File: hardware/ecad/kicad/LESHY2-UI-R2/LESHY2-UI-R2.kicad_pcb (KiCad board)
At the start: 6 copper layers, 80 x 150 mm, 432 parts, among them J1 Hirose FH34SRJ-50S-0.5SH(50), J10 Samtec FTSH-105-01-L-DV-K-P-TR, J11 GCT USB4105-GF-A, J12 GCT RFPC-SMA31-FN-175-A, J13 Hirose U.FL-R-SMT-1(80), J14 GCT RFPC-SMA31-FN-175-A, J15 Hirose U.FL-R-SMT-1(80), J16 GCT RFPC-SMA31-FN-175-A, J17 Hirose U.FL-R-SMT-1(80), J18 Hirose FX8C-80P-SV1(92), J2 Samtec FTSH-105-01-L-DV-K-P-TR, J3 GCT RFPC-SMA32-FN-175-A, J4 Hirose U.FL-R-SMT-1(80), J5 Hirose DM3AT-SF-PEJM5, J6 Samtec FTSH-105-01-L-DV-K-P-TR, J7 GCT RFPC-SMA32-FN-175-A, J8 Hirose U.FL-R-SMT-1(80), J9 GCT USB4105-GF-A, Q1 Diodes Incorporated DMN2056U-7, Q2 Diodes Incorporated 2N7002DW-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, Q3 Diodes Incorporated DMN2056U-7, Q4 Diodes Incorporated DMN2056U-7, Q5 Diodes Incorporated DMN2056U-7, Q6 Diodes Incorporated 2N7002DW-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, SW1 Alps Alpine SKRTLAE010, SW10 OMRON B3S-1100P, SW11 OMRON B3S-1100P, SW12 OMRON B3S-1100P, SW13 OMRON B3S-1100P, SW14 OMRON B3S-1100P, SW15 OMRON B3S-1100P, SW16 OMRON B3S-1100P, SW17 OMRON B3S-1100P, SW18 Alps Alpine SKRTLAE010, SW19 Alps Alpine SKRTLAE010, SW2 Alps Alpine SKRTLAE010, SW20 Alps Alpine SKRTLAE010, SW21 Alps Alpine SKRTLAE010, SW3 OMRON B3S-1100P, SW4 OMRON B3S-1100P, SW5 OMRON B3S-1100P, SW6 OMRON B3S-1100P, SW7 OMRON B3S-1100P, SW8 OMRON B3S-1100P, SW9 OMRON B3S-1100P, U1 ESP32-S3-WROOM-1U-N16R8, U10 Texas Instruments TPS22919DCKR, U11 SN74LVC1G07DCKR, U12 Texas Instruments TPD8E003DQDR, U13 TCA9539PWR, U14 ESP32-C5-WROOM-1U-N8R8, U15 Texas Instruments TPD4E05U06D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, U16 KYOCERA AVX CP0603Q5425ENTR, U17 74LVC2G14GV,125, U18 SN74LVC1G74DCUR, U19 74HC20PW,118, U2 Texas Instruments TPD4E05U06D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, U20 74LVC2G14GV,125, U21 Texas Instruments TPD2EUSB30A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, U22 onsemi FSUSB42MUX, U23 Vishay TSMP95000TR, U24 Vishay TSOP75238TR, U25 Texas Instruments TPS22919DCKR, U26 Nexperia 74LVC2G126DP,125, U27 SN74LVC1G08DCKR, U28 SC1512-A4, U29 Texas Instruments TPD4E05U06D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, U3 KYOCERA AVX CP0603Q5425ENTR, U30 Texas Instruments TPD2EUSB30A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, U31 onsemi FSUSB42MUX, U32 Analog Devices AD8314ARMZ-REEL, U33 Analog Devices AD8314ARMZ-REEL, U34 Analog Devices AD8314ARMZ-REEL, U35 Ebyte E01-ML01SP4, U36 TTM Technologies DC2337J5010A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, U37 Nexperia 74LVC126APW,118, U38 Nexperia 74LVC2G126DP,125, U39 Ebyte E01-ML01SP4, U4 Texas Instruments TPS2553DRVR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, U40 TTM Technologies DC2337J5010A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

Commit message: Protect C5 shared USB pair and document mux control gap
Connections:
- net /UI_20_C5_WIFI_IR_SERVICE/C5_GPIO13_COMMON renamed /UI_20_C5_WIFI_IR_SERVICE/C5_USB_SDIO_COMMON_N
- net /UI_20_C5_WIFI_IR_SERVICE/C5_GPIO14_COMMON renamed /UI_20_C5_WIFI_IR_SERVICE/C5_USB_SDIO_COMMON_P
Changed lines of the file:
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@@
 			(layers "B.Cu" "B.Mask" "B.Paste")
 			(roundrect_rratio 0.25)
-			(net "/UI_20_C5_WIFI_IR_SERVICE/C5_GPIO14_COMMON")
+			(net "/UI_20_C5_WIFI_IR_SERVICE/C5_USB_SDIO_COMMON_P")
 		)
 		(pad "4" smd roundrect
@@
 			(layers "B.Cu" "B.Mask" "B.Paste")
 			(roundrect_rratio 0.25)
-			(net "/UI_20_C5_WIFI_IR_SERVICE/C5_GPIO13_COMMON")
+			(net "/UI_20_C5_WIFI_IR_SERVICE/C5_USB_SDIO_COMMON_N")
 		)
 		(pad "5" smd roundrect
@@
 			(layers "B.Cu" "B.Mask" "B.Paste")
 			(roundrect_rratio 0.2)
-			(net "/UI_20_C5_WIFI_IR_SERVICE/C5_GPIO13_COMMON")
+			(net "/UI_20_C5_WIFI_IR_SERVICE/C5_USB_SDIO_COMMON_N")
 		)
 		(pad "14" smd roundrect
@@
 			(layers "B.Cu" "B.Mask" "B.Paste")
 			(roundrect_rratio 0.2)
-			(net "/UI_20_C5_WIFI_IR_SERVICE/C5_GPIO14_COMMON")
+			(net "/UI_20_C5_WIFI_IR_SERVICE/C5_USB_SDIO_COMMON_P")
 		)
 		(pad "15" smd roundrect

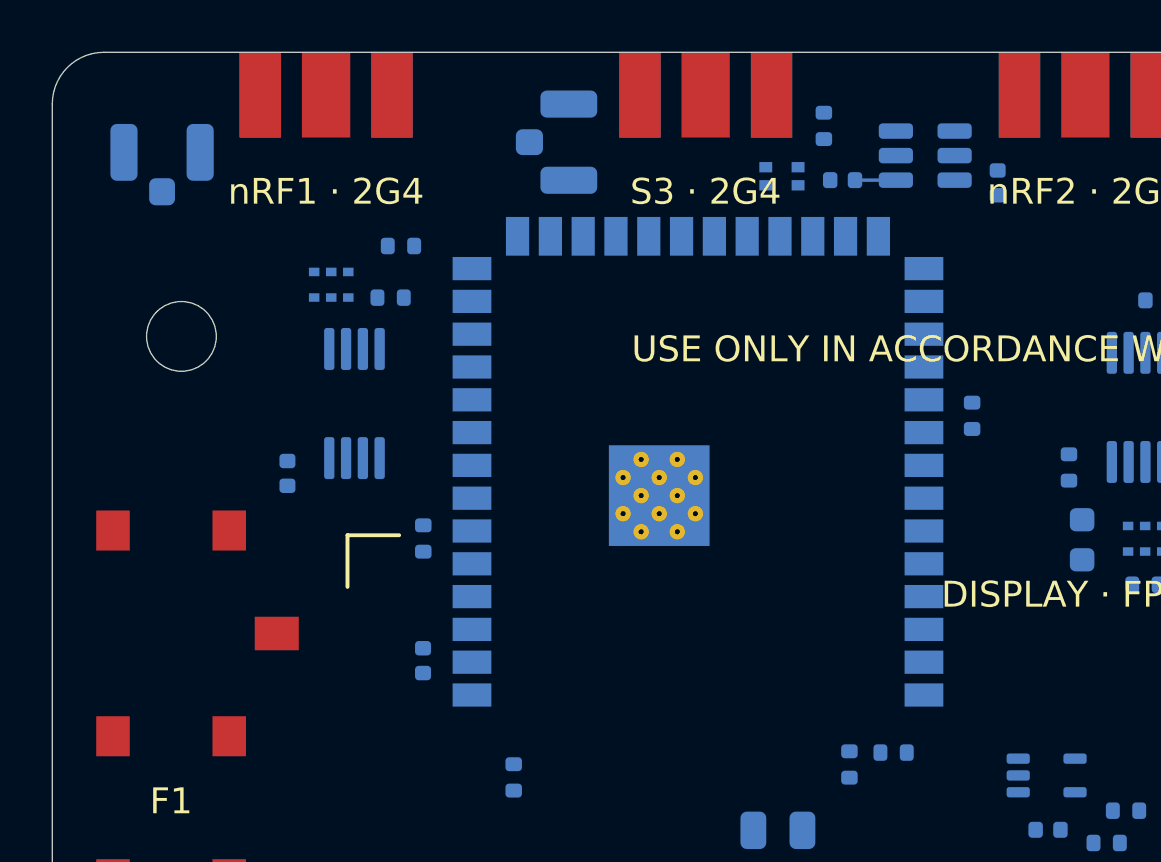
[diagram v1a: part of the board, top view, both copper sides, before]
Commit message: Clear SMA solder access with bounded support relocations
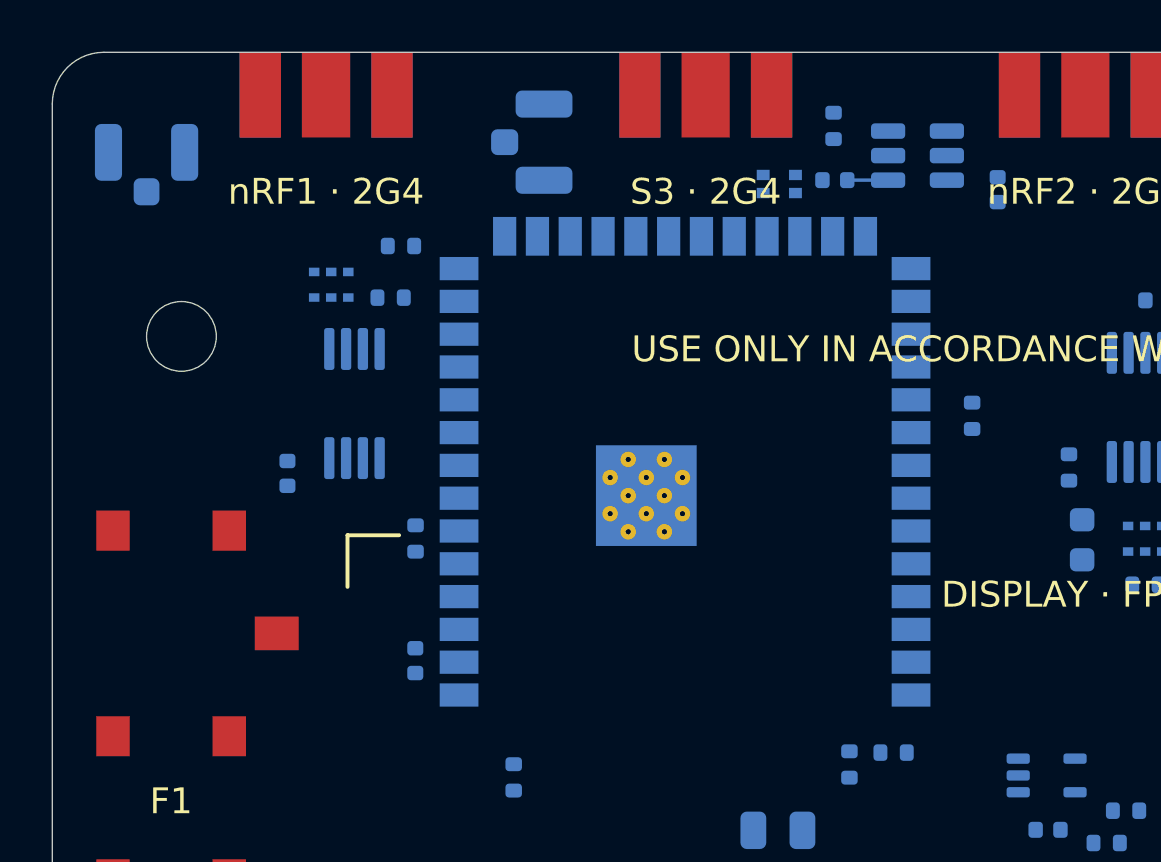
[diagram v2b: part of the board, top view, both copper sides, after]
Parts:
- moved J4 0.96 mm to (19.0, 3.48)
- moved J13 0.60 mm to (3.65, 3.88)
- moved U1 0.50 mm to (24.5, 16.5)
- moved R17 0.38 mm to (30.2, 2.85)
- moved U3 0.32 mm to (28.1, 5.10)
- moved C2 0.30 mm to (30.3, 4.95)
- moved C6 0.30 mm to (14.1, 23.6)
- moved R12 0.30 mm to (14.1, 18.8)
- moved U52 0.30 mm to (33.5, 4.00)
- moved C1 0.27 mm to (36.6, 5.32)

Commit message: fix(hardware): correct native placement and publish verified component views
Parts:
- moved C7 48.8 mm to (43.9, 40.4), turned to -90 degrees
- moved C15 45.3 mm to (66.8, 128.3), turned to 0 degrees
- moved C16 42.3 mm to (62.2, 130.3)
- moved C62 40.6 mm to (4.55, 52.2), turned to 180 degrees
- moved C63 32.0 mm to (5.17, 53.7), turned to 180 degrees
- moved C74 18.6 mm to (57.3, 62.0), turned to -90 degrees
- moved C68 17.3 mm to (30.1, 47.9), turned to 90 degrees
- moved C75 16.9 mm to (51.1, 57.6), turned to 180 degrees
- moved C69 14.8 mm to (29.9, 50.1), turned to 180 degrees
- moved C17 10.6 mm to (40.8, 78.4), turned to -90 degrees
- moved R18 10.0 mm to (53.9, 40.3), turned to 0 degrees
- moved R99 7.21 mm to (44.3, 60.1), turned to 180 degrees
- moved R198 6.28 mm to (44.8, 58.4), turned to 90 degrees
- moved R42 4.28 mm to (61.6, 126.1), turned to 90 degrees
- moved C54 0.30 mm to (14.8, 136.9)
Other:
- board text added: "SPEAKER / ASSEMBLY"

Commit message: Restore microphone to RF-inner bottom edge and align front label
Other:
- board text added: "MIC"
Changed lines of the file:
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@@
+		)
+	)
+	(gr_text "MIC"
+		(at 33 148.9 0)
+		(layer "F.SilkS")
+		(effects
+			(font
+				(size 1 1)
+				(thickness 0.15)
+			)
 		)
 	)

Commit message: Complete native interface silkscreen with verified local clearances
Add 29 real front/back labels and independently cover 76 interfaces / 95 required captions. Move eight reviewed unrouted RF resistors while preserving all native copper and named pad connectivity. Refresh four-face, exterior, and routing visuals; keep H6.0.3-R1 open.

Validation: system suite 1459 tests OK (114 skips in system Python); KiCad H6 suite 863 tests OK, no skips. Both native DRC reports have zero violations and zero schematic-parity errors. Current routing remains incomplete.
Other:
- board text added: "C5 ANT"
- board text added: "C5 DBG"
- board text added: "DISPLAY"
- board text added: "HUB DBG"
- board text added: "IR LRN"
- board text added: "IR RX"
- board text added: "IR TX"
- board text added: "M1 UI"
- board text added: "S3 ANT"
- board text added: "S3 DBG"
- board text added: "nRF1 ANT"
- board text added: "nRF2 ANT"
- board text added: "nRF3 ANT"
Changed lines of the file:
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@@
+		)
+	)
+	(gr_text "IR RX"
+		(at 4.5 78.1 0)
+		(layer "F.SilkS")
+		(effects
+			(font
+				(size 1 1)
+				(thickness 0.15)
+			)
+		)
+	)
+	(gr_text "IR LRN"
+		(at 4.5 85.6 0)
+		(layer "F.SilkS")
+		(effects
+			(font
+				(size 1 1)
+				(thickness 0.15)
+			)
+		)
+	)
+	(gr_text "IR TX"
+		(at 4.5 92 0)
+		(layer "F.SilkS")
+		(effects
+			(font
+				(size 1 1)
+				(thickness 0.15)
+			)
+		)
+	)
+	(gr_text "S3 DBG"
+		(at 3.075 109.6 0)
+		(layer "B.SilkS")
+		(effects
+			(font
+				(size 1 1)
+				(thickness 0.15)
+			)
+			(justify mirror)
+		)
+	)
+	(gr_text "nRF1 ANT"
+		(at 5 7.65 0)
+		(layer "B.SilkS")
+		(effects
+			(font
+				(size 1 1)
+				(thickness 0.15)
+			)
+			(justify mirror)
+		)
+	)
+	(gr_text "S3 ANT"
+		(at 24.04 5 0)
+		(layer "B.SilkS")
+		(effects
+			(font
+				(size 1 1)
+				(thickness 0.15)
+			)
+			(justify mirror)
+		)
+	)
+	(gr_text "C5 DBG"
+		(at 25.075 111.35 0)
+		(layer "B.SilkS")
+		(effects
+			(font
+				(size 1 1)
+				(thickness 0.15)
+			)
+			(justify mirror)
+		)
+	)
+	(gr_text "HUB DBG"
+		(at 35.275 140.35 0)
+		(layer "B.SilkS")
+		(effects
+			(font
+				(size 1 1)
+				(thickness 0.15)
+			)
+			(justify mirror)
+		)
+	)
+	(gr_text "M1 UI"
+		(at 43.5 127.35 0)
+		(layer "B.SilkS")
+		(effects
+			(font
+				(size 1 1)
+				(thickness 0.15)
+			)
+			(justify mirror)
+		)
+	)
+	(gr_text "nRF2 ANT"
+		(at 49.125 15.25 0)
+		(layer "B.SilkS")
+		(effects
+			(font
+				(size 1 1)
+				(thickness 0.15)
+			)
+			(justify mirror)
+		)
+	)
+	(gr_text "C5 ANT"
+		(at 57.575 14.25 0)
+		(layer "B.SilkS")
+		(effects
+			(font
+				(size 1 1)
+				(thickness 0.15)
+			)
+			(justify mirror)
+		)
+	)
+	(gr_text "nRF3 ANT"
+		(at 68 6.55 0)
+		(layer "B.SilkS")
+		(effects
+			(font
+				(size 1 1)
+				(thickness 0.15)
+			)
+			(justify mirror)
+		)
+	)
+	(gr_text "DISPLAY"
+		(at 31.5 40.9 90)
+		(layer "B.SilkS")
+		(effects
+			(font
+				(size 1 1)
+				(thickness 0.15)
+			)
+			(justify mirror)
 		)
 	)

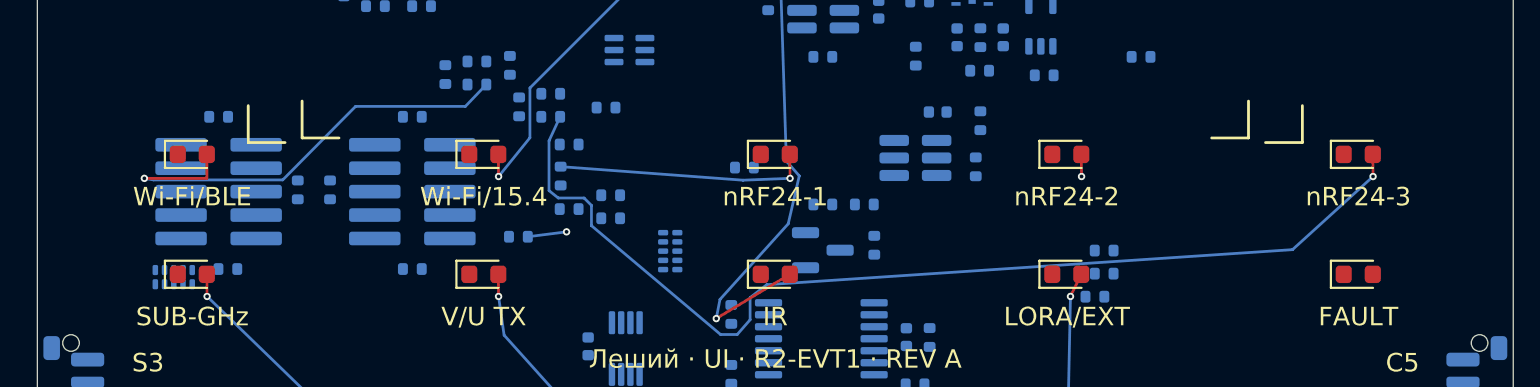
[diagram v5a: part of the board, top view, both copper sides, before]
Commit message: Increase display clearance above upper LED row
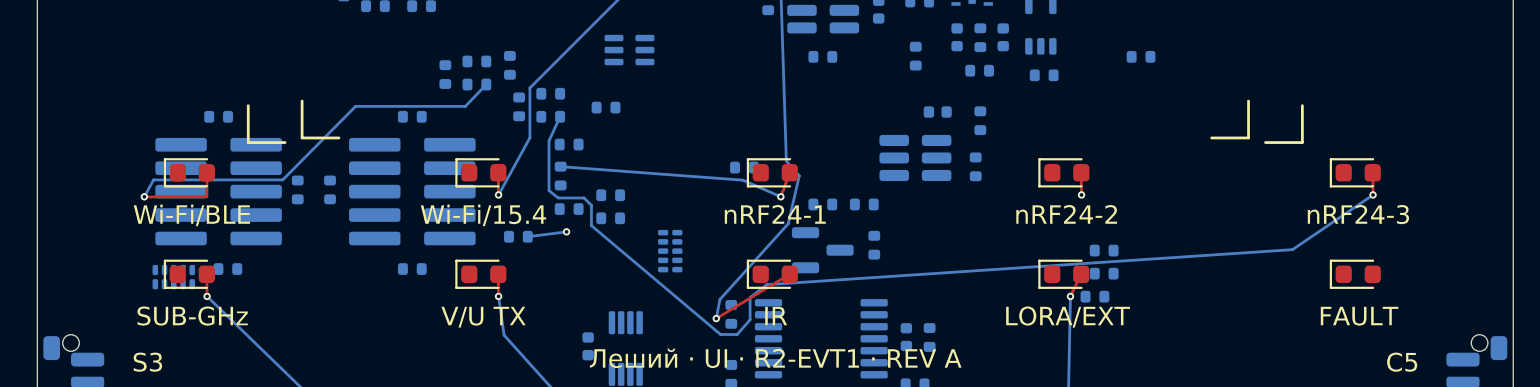
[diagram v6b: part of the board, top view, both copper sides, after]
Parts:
- moved D1 1.00 mm to (24.2, 105.9)
- moved D6 1.00 mm to (40.0, 105.9)
- moved D7 1.00 mm to (55.8, 105.9)
- moved D8 1.00 mm to (71.6, 105.9)
- moved D9 1.00 mm to (8.40, 105.9)
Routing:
- net /UI_11_STORAGE_CONTROLS_INDICATORS/C5_TX_LED_A: track 32.8 -> 33.7 mm
- net /UI_11_STORAGE_CONTROLS_INDICATORS/NRF2_TX_LED_A: track 57.0 -> 56.3 mm
- net /UI_11_STORAGE_CONTROLS_INDICATORS/S3_TX_LED_A: track 25.4 -> 25.9 mm
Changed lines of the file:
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@@
 	(footprint "LED_SMD:LED_0603_1608Metric"
 		(layer "F.Cu")
-		(at 8.4 104.9)
+		(at 8.4 105.9)
 		(descr "LED SMD 0603 (1608 Metric), square (rectangular) end terminal, IPC-7351 nominal, (Body size source: http://www.tortai-tech.com/upload/download/2011102023233369053.pdf)")
 		(tags "LED")
@@
 				(font
 					(size 1.27 1.27)
-					(thickness 0.15)
 				)
 			)
@@
 	(footprint "LED_SMD:LED_0603_1608Metric"
 		(layer "F.Cu")
-		(at 40 104.9)
+		(at 40 105.9)
 		(descr "LED SMD 0603 (1608 Metric), square (rectangular) end terminal, IPC-7351 nominal, (Body size source: http://www.tortai-tech.com/upload/download/2011102023233369053.pdf)")
 		(tags "LED")
@@
 				(font
 					(size 1.27 1.27)
-					(thickness 0.15)
 				)
 			)
@@
 	(footprint "LED_SMD:LED_0603_1608Metric"
 		(layer "F.Cu")
-		(at 71.6 104.9)
+		(at 71.6 105.9)
 		(descr "LED SMD 0603 (1608 Metric), square (rectangular) end terminal, IPC-7351 nominal, (Body size source: http://www.tortai-tech.com/upload/download/2011102023233369053.pdf)")
 		(tags "LED")
@@
 				(font
 					(size 1.27 1.27)
-					(thickness 0.15)
 				)
 			)
@@
 	(footprint "LED_SMD:LED_0603_1608Metric"
 		(layer "F.Cu")
-		(at 55.8 104.9)
+		(at 55.8 105.9)
 		(descr "LED SMD 0603 (1608 Metric), square (rectangular) end terminal, IPC-7351 nominal, (Body size source: http://www.tortai-tech.com/upload/download/2011102023233369053.pdf)")
 		(tags "LED")
@@
 				(font
 					(size 1.27 1.27)
-					(thickness 0.15)
 				)
 			)
@@
 	(footprint "LED_SMD:LED_0603_1608Metric"
 		(layer "F.Cu")
-		(at 24.2 104.9)
+		(at 24.2 105.9)
 		(descr "LED SMD 0603 (1608 Metric), square (rectangular) end terminal, IPC-7351 nominal, (Body size source: http://www.tortai-tech.com/upload/download/2011102023233369053.pdf)")
 		(tags "LED")
@@
 				(font
 					(size 1.27 1.27)
-					(thickness 0.15)
 				)
 			)
@@
 		)
 	)
-	(gr_text "Wi-Fi/BLE"
-		(at 8.4 107.2 0)
-		(layer "F.SilkS")
-		(effects
-			(font
-				(size 1 1)
-				(thickness 0.15)
-			)
-		)
-	)
 	(gr_text "SUB-GHz"
 		(at 8.4 113.7 0)
@@
 		)
 	)
-	(gr_text "Wi-Fi/15.4"
-		(at 24.2 107.2 0)
-		(layer "F.SilkS")
-		(effects
-			(font
-				(size 1 1)
-				(thickness 0.15)
-			)
-		)
-	)
 	(gr_text "V/U TX"
 		(at 24.2 113.7 0)
@@
 		)
 	)
-	(gr_text "nRF24-1"
-		(at 40 107.2 0)
-		(layer "F.SilkS")
-		(effects
-			(font
-				(size 1 1)
-				(thickness 0.15)
-			)
-		)
-	)
 	(gr_text "IR"
 		(at 40 113.7 0)
@@
 		)
 	)
-	(gr_text "nRF24-2"
-		(at 55.8 107.2 0)
-		(layer "F.SilkS")
-		(effects
-			(font
-				(size 1 1)
-				(thickness 0.15)
-			)
-		)
-	)
 	(gr_text "LORA/EXT"
 		(at 55.8 113.7 0)
@@
 		)
 	)
-	(gr_text "nRF24-3"
-		(at 71.6 107.2 0)
-		(layer "F.SilkS")
-		(effects
-			(font
-				(size 1 1)
-				(thickness 0.15)
-			)
-		)
-	)
 	(gr_text "FAULT"
 		(at 71.6 113.7 0)
@@
 	)
 	(segment
-		(start 9.1875 106.2)
-		(end 5.8 106.2)
+		(start 9.1875 107.2)
+		(end 5.8 107.2)
 		(width 0.15)
 		(layer "F.Cu")
@@
 	)
 	(segment
-		(start 9.1875 104.9)
-		(end 9.1875 106.2)
+		(start 9.1875 105.9)
+		(end 9.1875 107.2)
 		(width 0.15)
 		(layer "F.Cu")
@@
 	(segment
 		(start 38.25 106.3)
-		(end 40.8 106.2)
+		(end 40.3 107.2)
 		(width 0.15)
 		(layer "B.Cu")
@@
 	)
 	(via
-		(at 40.8 106.2)
+		(at 40.3 107.2)
 		(size 0.4)
 		(drill 0.2)
@@
 	(segment
 		(start 6.3 106.285)
-		(end 5.8 106.2)
+		(end 5.8 107.2)
 		(width 0.15)
 		(layer "B.Cu")
@@
 	)
 	(segment
-		(start 40.7875 104.9)
-		(end 40.8 106.2)
+		(start 40.7875 105.9)
+		(end 40.3 107.2)
 		(width 0.15)
 		(layer "F.Cu")
@@
 	)
 	(via
-		(at 5.8 106.2)
+		(at 5.8 107.2)
 		(size 0.4)
 		(drill 0.2)
@@
 	(segment
 		(start 26.7 104)
-		(end 25 106.1)
+		(end 25 107.1)
 		(width 0.15)
 		(layer "B.Cu")
@@
 	)
 	(via
-		(at 25 106.1)
+		(at 25 107.1)
 		(size 0.4)
 		(drill 0.2)
@@
 	(segment
 		(start 68.035 110.065)
-		(end 72.4 106.1)
+		(end 72.4 107.1)
 		(width 0.15)
 		(layer "B.Cu")
@@
 	)
 	(via
-		(at 72.4 106.1)
+		(at 72.4 107.1)
 		(size 0.4)
 		(drill 0.2)
@@
 	(segment
 		(start 28.685 109.1)
-		(end 56.6 106.1)
+		(end 56.6 107.1)
 		(width 0.15)
 		(layer "In2.Cu")
@@
 	)
 	(via
-		(at 56.6 106.1)
+		(at 56.6 107.1)
 		(size 0.4)
 		(drill 0.2)
@@
 	)
 	(segment
-		(start 24.9875 104.9)
-		(end 25 106.1)
+		(start 24.9875 105.9)
+		(end 25 107.1)
 		(width 0.15)
 		(layer "F.Cu")
@@
 	)
 	(segment
-		(start 56.5875 104.9)
-		(end 56.6 106.1)
+		(start 56.5875 105.9)
+		(end 56.6 107.1)
 		(width 0.15)
 		(layer "F.Cu")
@@
 	)
 	(segment
-		(start 72.3875 104.9)
-		(end 72.4 106.1)
+		(start 72.3875 105.9)
+		(end 72.4 107.1)
 		(width 0.15)
 		(layer "F.Cu")
@@
 		)
 	)
+	(gr_text "Wi-Fi/BLE"
+		(at 8.4 108.2 0)
+		(layer "F.SilkS")
+		(effects
+			(font
+				(size 1 1)
+				(thickness 0.15)
+			)
+		)
+	)
+	(gr_text "Wi-Fi/15.4"
+		(at 24.2 108.2 0)
+		(layer "F.SilkS")
+		(effects
+			(font
+				(size 1 1)
+				(thickness 0.15)
+			)
+		)
+	)
+	(gr_text "nRF24-1"
+		(at 40 108.2 0)
+		(layer "F.SilkS")
+		(effects
+			(font
+				(size 1 1)
+				(thickness 0.15)
+			)
+		)
+	)
+	(gr_text "nRF24-2"
+		(at 55.8 108.2 0)
+		(layer "F.SilkS")
+		(effects
+			(font
+				(size 1 1)
+				(thickness 0.15)
+			)
+		)
+	)
+	(gr_text "nRF24-3"
+		(at 71.6 108.2 0)
+		(layer "F.SilkS")
+		(effects
+			(font
+				(size 1 1)
+				(thickness 0.15)
+			)
+		)
+	)

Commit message: Restore C5 BOOT net and verify current recovery boundaries
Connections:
- U14 pad 15: (no net) -> /UI_20_C5_WIFI_IR_SERVICE/C5_BOOT_N
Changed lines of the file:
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@@
 			(layers "B.Cu" "B.Mask" "B.Paste")
 			(roundrect_rratio 0.2)
+			(net "/UI_20_C5_WIFI_IR_SERVICE/C5_BOOT_N")
 		)
 		(pad "16" smd roundrect
